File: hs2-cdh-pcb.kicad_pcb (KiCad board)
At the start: 2 copper layers, 86.4 x 54.6 mm, 6 parts, among them P8 BeagleBone_Black_Header, P9 BeagleBone_Black_Header

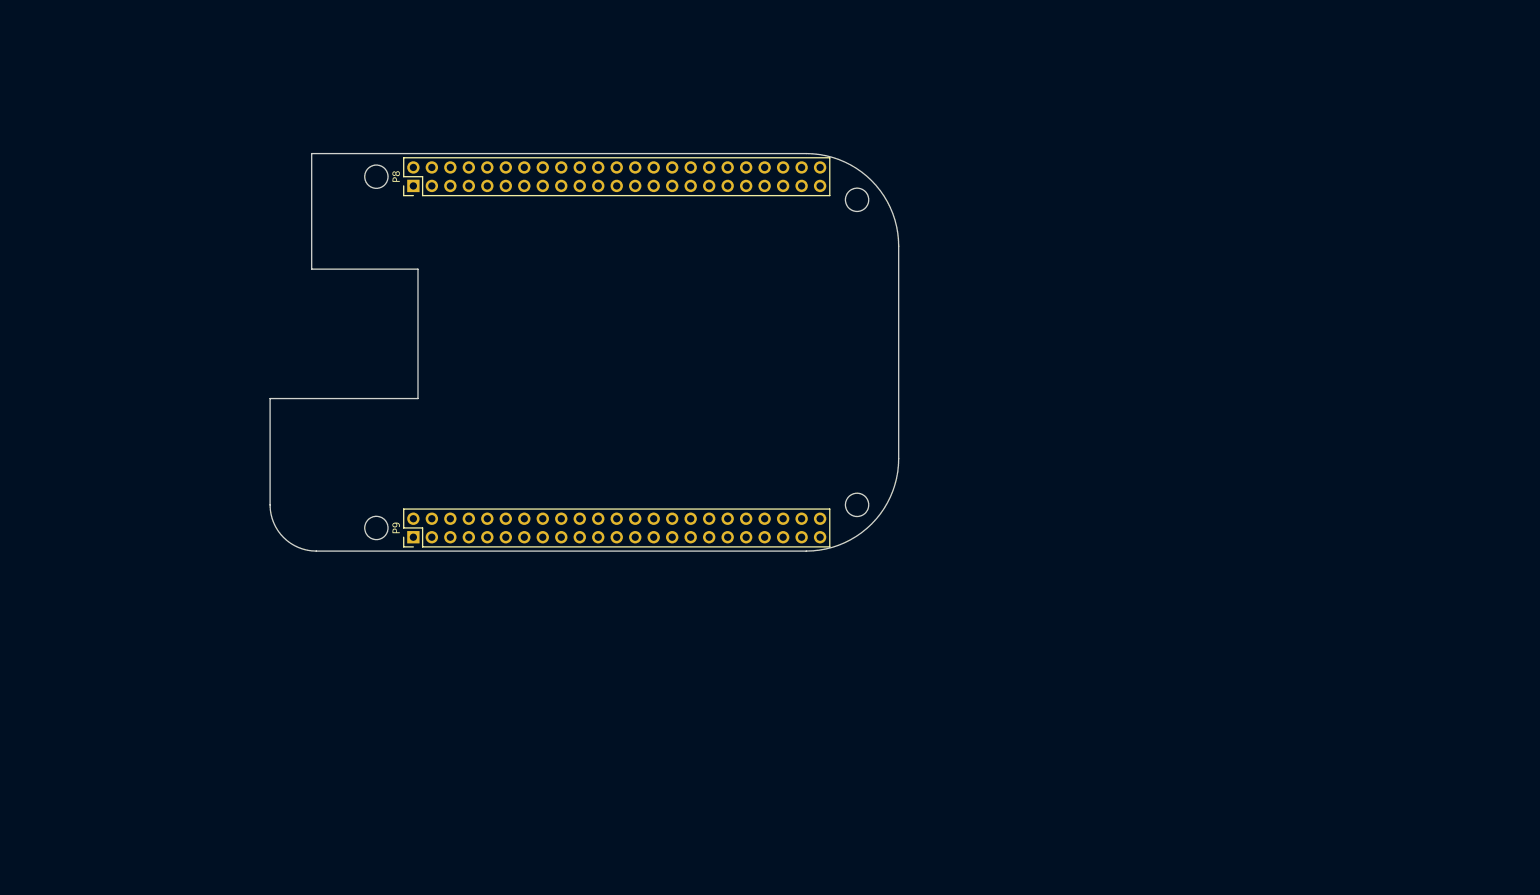
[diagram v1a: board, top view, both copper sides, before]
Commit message: Merge Payload and thermals
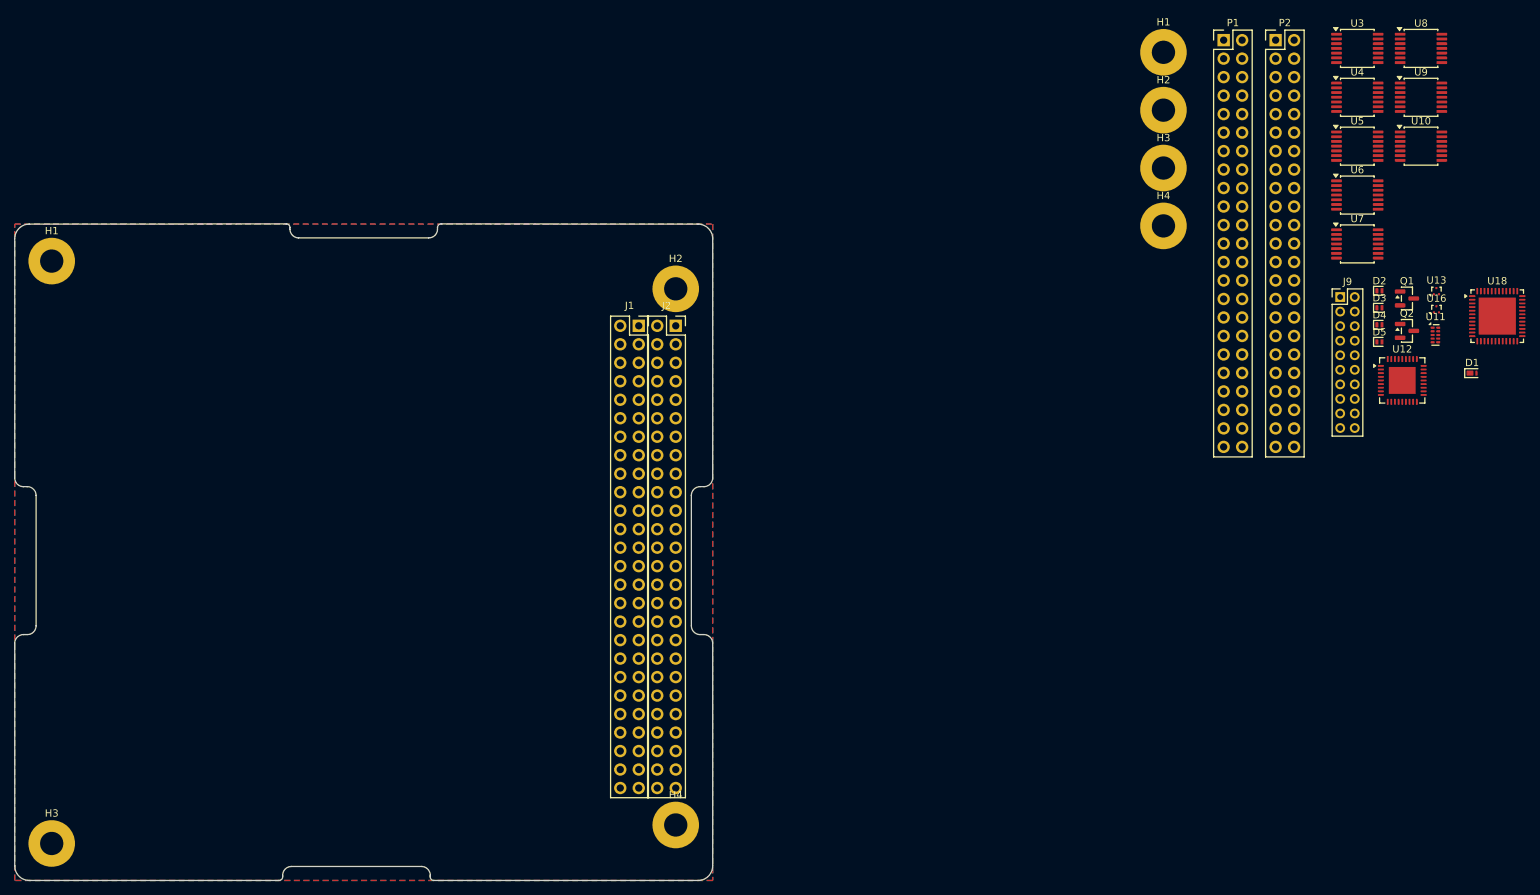
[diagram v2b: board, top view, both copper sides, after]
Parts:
- removed MH1, MH2, MH3, MH4: MountingHole_3.2mm_M3_DIN965, MountingHole:MountingHole_3.2mm_M3_DIN965
- removed P8, P9: BeagleBone_Black_Header, Connector_PinHeader_2.54mm:PinHeader_2x23_P2.54mm_Vertical
- added D1: TBD, Diode_SMD:Nexperia_DSN1608-2_1.6x0.8mm, F.Cu at (265.1, 75.6)
- added D2: PESD5V0L1UL, Diode_SMD:D_SOD-882, F.Cu at (252.4, 64.2)
- added D3: PESD5V0L1UL, Diode_SMD:D_SOD-882, F.Cu at (252.4, 66.6)
- added D4: PESD5V0L1UL, Diode_SMD:D_SOD-882, F.Cu at (252.4, 68.9)
- added D5: PESD5V0L1UL, Diode_SMD:D_SOD-882, F.Cu at (252.4, 71.3)
- added H1: MountingHole_Pad, MountingHole:MountingHole_3.2mm_M3_Pad, F.Cu at (222.7, 31.5)
- added H1: MountingHole_Pad, MountingHole:MountingHole_3.2mm_M3_Pad, F.Cu at (70.0, 60.2)
- added H2: MountingHole_Pad, MountingHole:MountingHole_3.2mm_M3_Pad, F.Cu at (155.7, 64.0)
- added H2: MountingHole_Pad, MountingHole:MountingHole_3.2mm_M3_Pad, F.Cu at (222.7, 39.4)
- added H3: MountingHole_Pad, MountingHole:MountingHole_3.2mm_M3_Pad, F.Cu at (70.0, 140.2)
- added H3: MountingHole_Pad, MountingHole:MountingHole_3.2mm_M3_Pad, F.Cu at (222.7, 47.4)
- added H4: MountingHole_Pad, MountingHole:MountingHole_3.2mm_M3_Pad, F.Cu at (155.7, 137.6)
- added H4: MountingHole_Pad, MountingHole:MountingHole_3.2mm_M3_Pad, F.Cu at (222.7, 55.3)
- added J1: Conn_02x26_Row_Letter_First, Connector_PinSocket_2.54mm:PinSocket_2x26_P2.54mm_Vertical, F.Cu at (150.7, 69.0)
- added J2: Conn_02x26_Row_Letter_First, Connector_PinSocket_2.54mm:PinSocket_2x26_P2.54mm_Vertical, F.Cu at (155.7, 69.0)
- added J9: Conn_02x10_Odd_Even, Connector_PinHeader_2.00mm:PinHeader_2x10_P2.00mm_Vertical, F.Cu at (247.0, 65.1)
- added P1: BeagleBone_Black_Header, Connector_PinHeader_2.54mm:PinHeader_2x23_P2.54mm_Vertical, F.Cu at (231.0, 29.8)
- added P2: BeagleBone_Black_Header, Connector_PinHeader_2.54mm:PinHeader_2x23_P2.54mm_Vertical, F.Cu at (238.1, 29.8)
- added Q1: BSS138, Package_TO_SOT_SMD:SOT-23, F.Cu at (256.2, 65.3)
- added Q2: BSS138, Package_TO_SOT_SMD:SOT-23, F.Cu at (256.2, 69.7)
- added U10: MAX31856, Package_SO:TSSOP-14_4.4x5mm_P0.65mm, F.Cu at (258.1, 44.4)
- added U11: TPD4E02B04DQA, Package_SON:USON-10_2.5x1.0mm_P0.5mm, F.Cu at (260.1, 70.3)
- added U12: USB2514B_Bi, Package_DFN_QFN:QFN-36-1EP_6x6mm_P0.5mm_EP3.7x3.7mm, F.Cu at (255.5, 76.6)
- added U13: TPD2EUSB30A, Package_TO_SOT_SMD:Texas_DRT-3, F.Cu at (260.2, 64.3)
- added U16: TPD2EUSB30A, Package_TO_SOT_SMD:Texas_DRT-3, F.Cu at (260.2, 66.8)
- added U18: MAX14830, Package_DFN_QFN:TQFN-48-1EP_7x7mm_P0.5mm_EP5.1x5.1mm, F.Cu at (268.6, 67.7)
- added U3: MAX31856, Package_SO:TSSOP-14_4.4x5mm_P0.65mm, F.Cu at (249.4, 30.9)
- added U4: MAX31856, Package_SO:TSSOP-14_4.4x5mm_P0.65mm, F.Cu at (249.4, 37.7)
- added U5: MAX31856, Package_SO:TSSOP-14_4.4x5mm_P0.65mm, F.Cu at (249.4, 44.4)
- added U6: MAX31856, Package_SO:TSSOP-14_4.4x5mm_P0.65mm, F.Cu at (249.4, 51.1)
- added U7: MAX31856, Package_SO:TSSOP-14_4.4x5mm_P0.65mm, F.Cu at (249.4, 57.8)
- added U8: MAX31856, Package_SO:TSSOP-14_4.4x5mm_P0.65mm, F.Cu at (258.1, 30.9)
- added U9: MAX31856, Package_SO:TSSOP-14_4.4x5mm_P0.65mm, F.Cu at (258.1, 37.7)
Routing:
- added copper zone on B.Cu, net GND
- added copper zone on F.Cu, net GND
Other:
- board size 86.4 x 54.6 mm -> 95.9 x 90.2 mm
- board text removed: "Note: due to to way pin numbers work on the BBB, the connectors are actually 2.54mm pin headers with the 3D models overridden."
